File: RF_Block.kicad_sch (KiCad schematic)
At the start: 10 parts, among them J12 Conn_Coaxial, U10 DLF162500LT-5028A1

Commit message: Layout draft complete
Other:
- note removed: "https://www.st.com/resource/en/user_manual/um2435-bluetooth-low-energy-and-802154-nucleo-pack-based-on-stm32wb-series-microcontrollers-stmicroelectronics.pdf"
- title: (none) -> Jakka1
- moved on the sheet: ANT1, C15, C43, C44, J12, L3, L6, L7, R42, U10

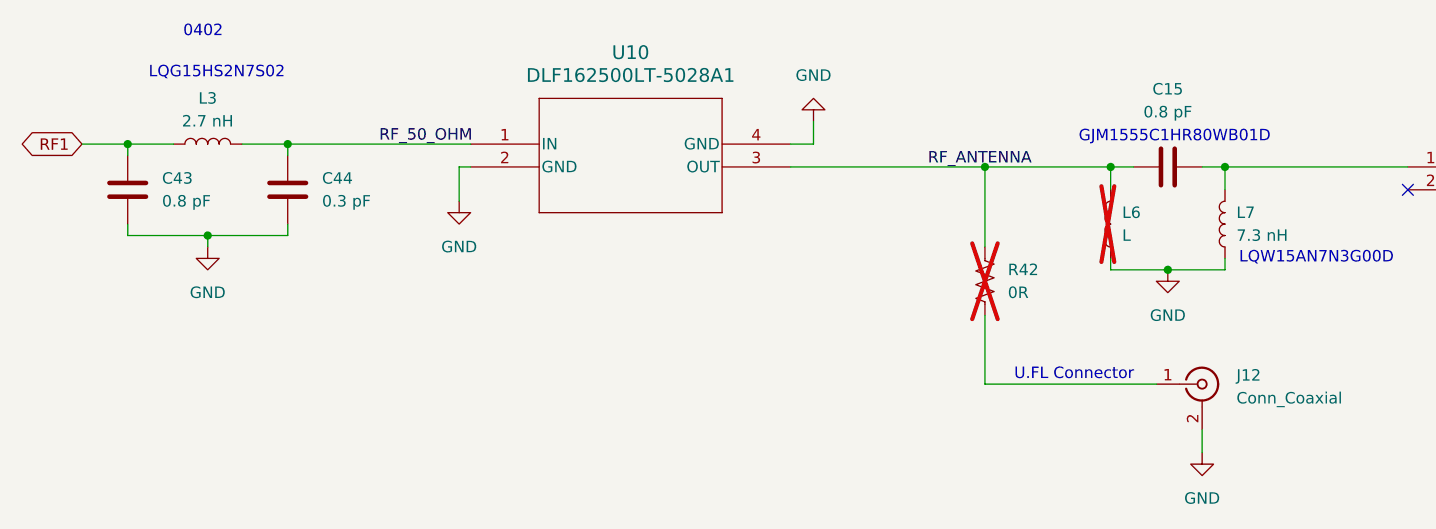
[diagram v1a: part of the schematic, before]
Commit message: First draft of design output, schematic, and layout complete
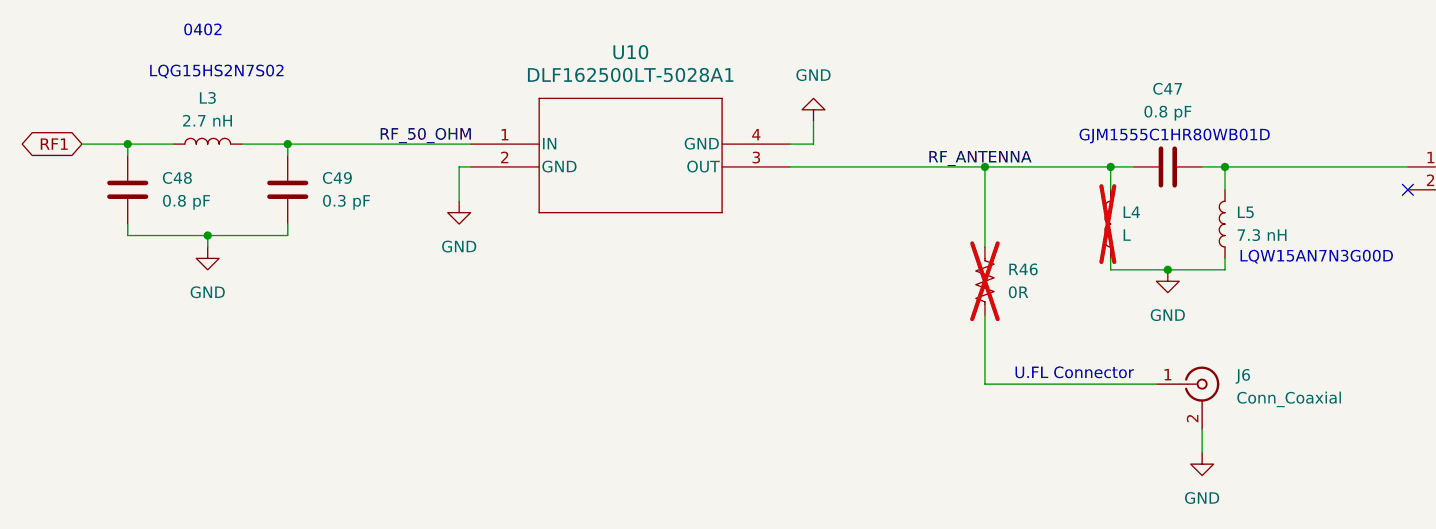
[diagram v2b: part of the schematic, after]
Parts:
- renumbered C15 to C47, C43 to C48, C44 to C49, J12 to J6, L6 to L4, L7 to L5, R42 to R46
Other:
- company: (none) -> Jacob Kapala
